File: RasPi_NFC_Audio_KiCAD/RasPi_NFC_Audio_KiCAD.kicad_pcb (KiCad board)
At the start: 2 copper layers, 103.5 x 65 mm, 72 parts, among them J1 Barrel_Jack_Switch, J2 Conn_02x20_Odd_Even, J4 Screw_Terminal_01x02, J5 Screw_Terminal_01x02, U1 MIC5225-3.3V, U2 PN532, U3 MAX98357, U4 MAX98357, Y1 Oscillator

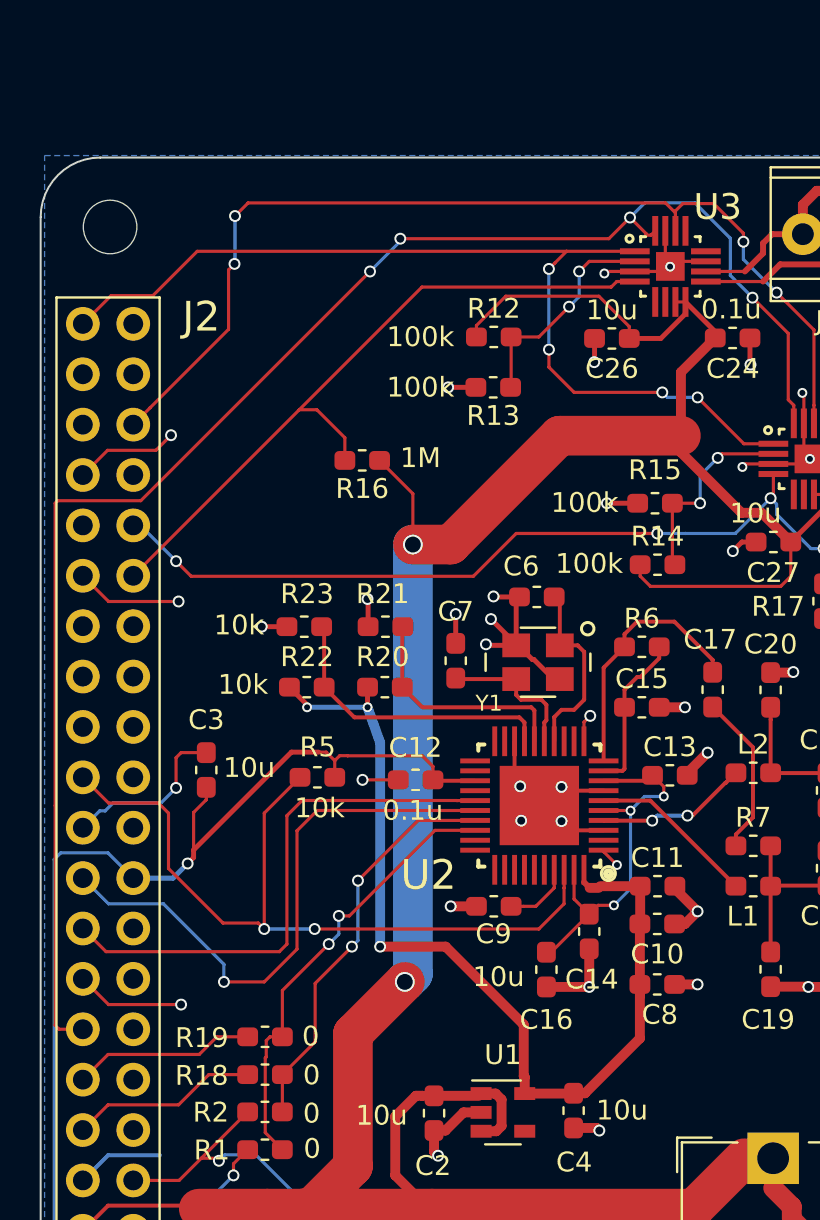
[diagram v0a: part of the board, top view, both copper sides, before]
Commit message: Added GPIO expander to schematic
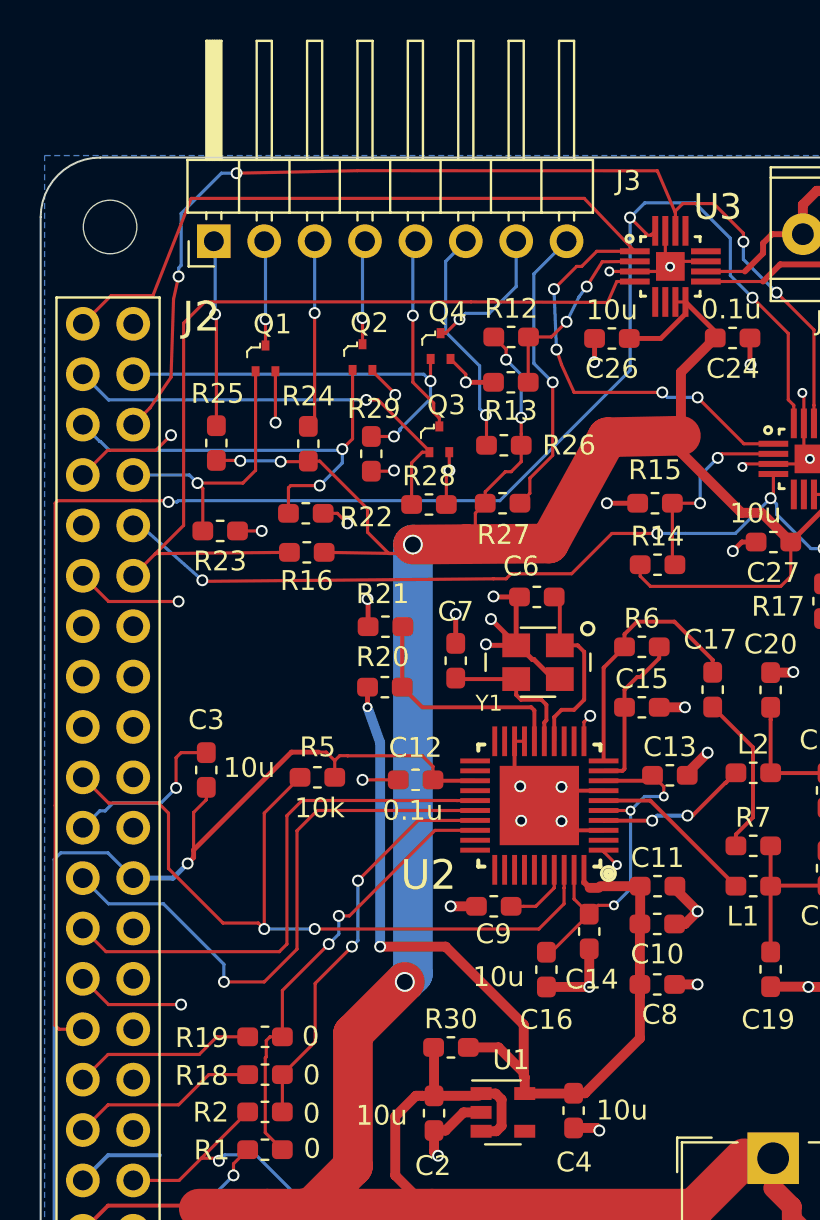
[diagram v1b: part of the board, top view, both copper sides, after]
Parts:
- added J3: Conn_01x08, Connector_PinHeader_2.54mm:PinHeader_1x08_P2.54mm_Horizontal, F.Cu at (117.2, 52.5)
- added Q1: DMG1012T-7, digikey-footprints:SOT-523, F.Cu at (119.8, 58.4)
- added Q2: DMG1012T-7, digikey-footprints:SOT-523, F.Cu at (124.7, 58.3)
- added Q3: DMG1012T-7, digikey-footprints:SOT-523, F.Cu at (128.6, 62.4)
- added Q4: DMG1012T-7, digikey-footprints:SOT-523, F.Cu at (128.6, 57.7)
- added R24: 121, Resistor_SMD:R_0603_1608Metric_Pad1.05x0.95mm_HandSolder, F.Cu at (122.0, 62.7)
- added R25: 121, Resistor_SMD:R_0603_1608Metric_Pad1.05x0.95mm_HandSolder, F.Cu at (117.3, 62.6)
- added R26: 121, Resistor_SMD:R_0603_1608Metric_Pad1.05x0.95mm_HandSolder, F.Cu at (131.8, 62.8)
- added R27: 121, Resistor_SMD:R_0603_1608Metric_Pad1.05x0.95mm_HandSolder, F.Cu at (131.8, 65.7)
- added R28: 10k, Resistor_SMD:R_0603_1608Metric_Pad1.05x0.95mm_HandSolder, F.Cu at (128.0, 65.7)
- added R29: 10k, Resistor_SMD:R_0603_1608Metric_Pad1.05x0.95mm_HandSolder, F.Cu at (125.1, 63.2)
- added R30: 0, Resistor_SMD:R_0603_1608Metric_Pad1.05x0.95mm_HandSolder, F.Cu at (129.1, 93.1)
- moved R22 8.76 mm to (121.8, 66.2)
- moved R23 6.42 mm to (117.5, 67.1), turned to 0 degrees
- moved R16 5.41 mm to (121.9, 68.1)
- moved R13 0.92 mm to (132.2, 59.6)
- moved R12 0.88 mm to (132.2, 57.3)
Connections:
- C10 pad 1: +3V3 -> +BATT
- C11 pad 1: +3V3 -> +BATT
- C4 pad 1: +3V3 -> +BATT
- C8 pad 1: +3V3 -> +BATT
- J2 pad 33: /GPIO13(PWM1) -> LED_0
- J2 pad 36: /GPIO16 -> LED_1
- J2 pad 37: /GPIO26 -> LED_3
- J2 pad 38: /GPIO20(SPI1_MOSI) -> LED_2
- R20 pad 1: +3V3 -> +BATT
- R22 pad 1: +3V3 -> LED_1
- R22 pad 2: SEL1 -> GND
- R23 pad 1: SEL1 -> LED_0
- U1 pad 5: +3V3 -> +BATT
- U2 pad 17: SEL1 -> GND
- U2 pad 40: +3V3 -> +BATT
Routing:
- net +3V3: track 48.2 -> 0.00 mm, vias 3 -> 0
- net +BATT: track 0.00 -> 47.1 mm, vias 0 -> 2
- net LED_1: track 0.00 -> 23.1 mm, vias 0 -> 2
- net LED_2: track 0.00 -> 22.3 mm, vias 0 -> 1
- net LED_3: track 0.00 -> 20.9 mm, vias 0 -> 2
- net +5V: track 199.5 -> 216.6 mm, vias 2 -> 6
- net Net-(J3-Pad8): track 0.00 -> 15.0 mm, vias 0 -> 1
- net SEL1: track 14.9 -> 0.00 mm
- net LED_0: track 0.00 -> 14.1 mm, vias 0 -> 1
- net GND: track 140.3 -> 151.9 mm, vias 47 -> 52
- net Net-(J3-Pad6): track 0.00 -> 11.6 mm, vias 0 -> 1
- net Net-(J3-Pad5): track 0.00 -> 9.94 mm, vias 0 -> 1
- net Net-(J3-Pad3): track 0.00 -> 9.56 mm, vias 0 -> 1
- net Net-(J3-Pad1): track 0.00 -> 9.35 mm, vias 0 -> 1
- net AUDIO_SD_N_0: track 35.5 -> 44.4 mm
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
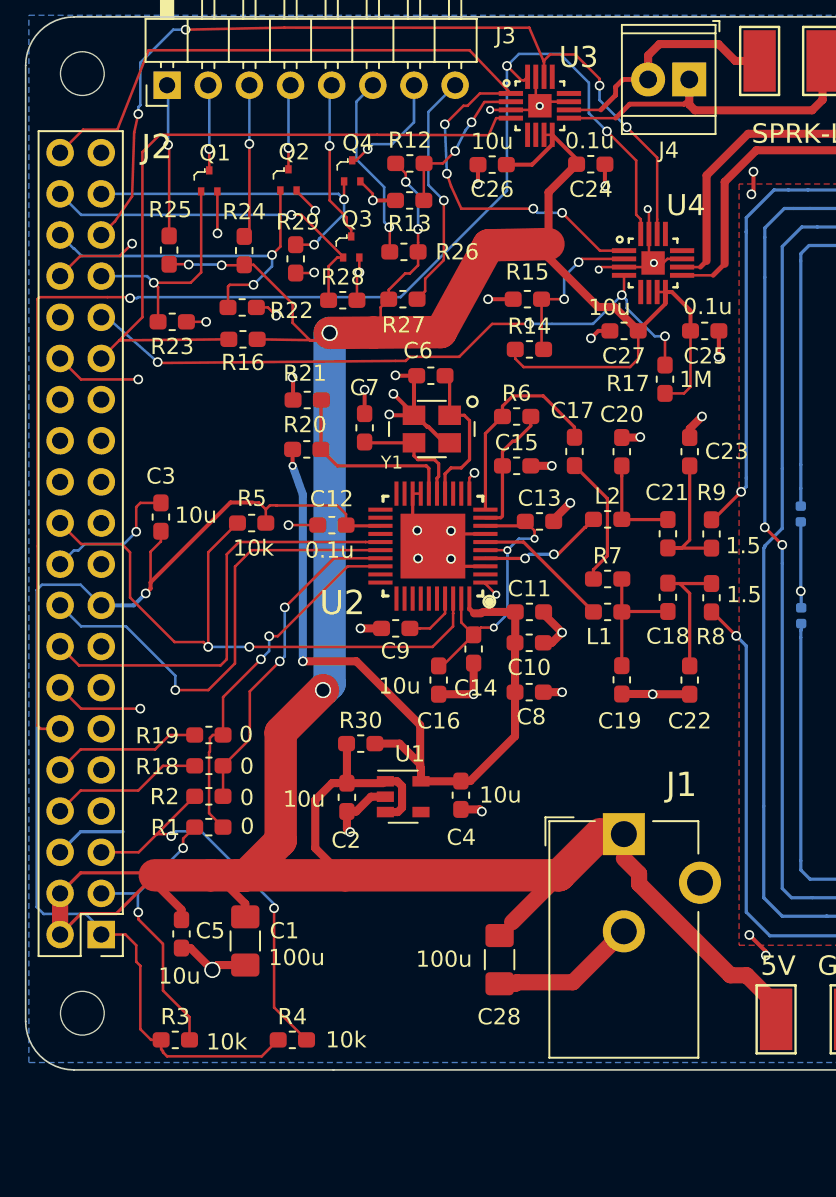
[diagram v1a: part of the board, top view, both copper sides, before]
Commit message: Updated layout for GPIO expander
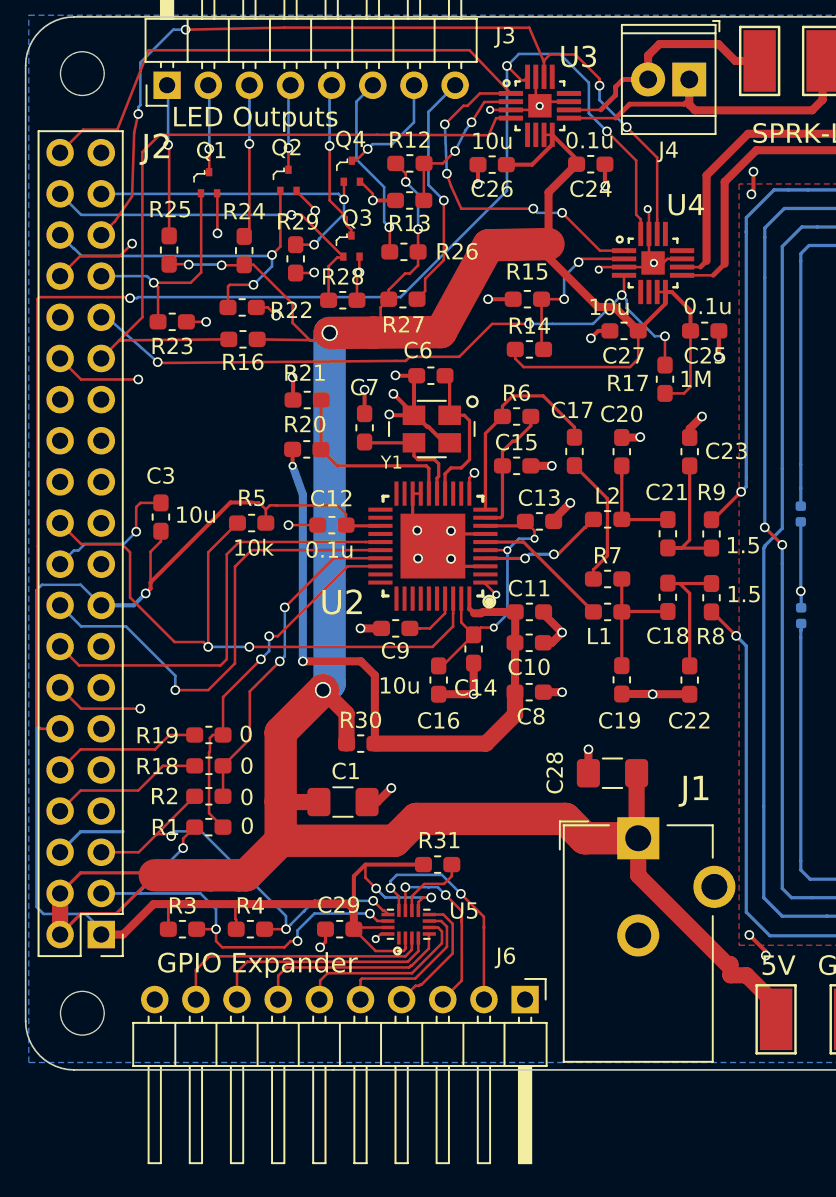
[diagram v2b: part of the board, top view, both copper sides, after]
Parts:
- removed C2, C4, C5: 10u, Capacitor_SMD:C_0603_1608Metric_Pad1.05x0.95mm_HandSolder
- removed U1: MIC5225-3.3V, Package_TO_SOT_SMD:SOT-23-5
- added C29: 0.1u, Capacitor_SMD:C_0603_1608Metric_Pad1.05x0.95mm_HandSolder, F.Cu at (127.8, 104.6)
- added J6: Conn_01x10, Connector_PinHeader_2.54mm:PinHeader_1x10_P2.54mm_Horizontal, F.Cu at (139.3, 108.9)
- added R31: 10k, Resistor_SMD:R_0603_1608Metric_Pad1.05x0.95mm_HandSolder, F.Cu at (133.9, 100.6)
- added U5: FXL6408UMX, RasPi_NFC_Audio_PCB_Lib:QFN40P260X180X55-16N, F.Cu at (132.1, 104.3)
- Q1, Q2, Q3, Q4: footprint digikey-footprints:SOT-523 -> RasPi_NFC_Audio_PCB_Lib:SOT-523
- moved C28 13.5 mm to (144.7, 94.9), turned to 180 degrees
- moved C1 10.5 mm to (128.1, 96.7), turned to 0 degrees
- moved R4 7.31 mm to (122.3, 104.6)
- moved R3 6.85 mm to (118.1, 104.6)
- moved J1 0.92 mm to (146.3, 98.9)
- moved Q1 0.12 mm to (119.8, 58.5)
- moved Q3 0.05 mm to (128.6, 62.4)
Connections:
- net /GPIO2(SDA1) renamed I2C_SDA
- net /GPIO3(SCL1) renamed I2C_SCL
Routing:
- net VCOM: track 72.4 -> 95.6 mm, vias 1 -> 3
- net +5V: track 216.6 -> 196.9 mm
- net GPIO_XPDR_7: track 0.00 -> 16.4 mm
- net GPIO_XPDR_6: track 0.00 -> 14.2 mm
- net GPIO_XPDR_0: track 0.00 -> 14.2 mm, vias 0 -> 2
- net GND: track 151.9 -> 138.3 mm, vias 52 -> 53
- net GPIO_XPDR_5: track 0.00 -> 12.4 mm
- net GPIO_XPDR_1: track 0.00 -> 11.6 mm, vias 0 -> 2
- net GPIO_XPDR_4: track 0.00 -> 11.3 mm
- net I2C_SDA: track 18.2 -> 28.4 mm, vias 2 -> 4
- net GPIO_XPDR_3: track 0.00 -> 9.89 mm
- net GPIO_XPDR_2: track 0.00 -> 7.86 mm
- net +BATT: track 47.1 -> 41.6 mm
- net Net-(R31-Pad2): track 0.00 -> 4.57 mm
- net I2C_SCL: track 25.7 -> 27.1 mm, vias 2 -> 3
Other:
- rule trace_min: 0.16 -> 0.15
- board text added: "GPIO Expander"
- board text added: "LED Outputs"
